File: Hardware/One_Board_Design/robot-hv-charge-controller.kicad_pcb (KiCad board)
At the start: 2 copper layers, 100 x 100 mm, 132 parts, among them J1 USB2.0_16P, J2 UART_CONN, J3 XT30PW-M, J4 Conn_01x02, J5 XT60PW-M, J6 Conn_01x02, J7 XT60PW-M, J8 Conn_01x03, J9 Conn_01x02, Q2 2SD882, Q3 BC817, Q4 BC817, Q5 2SD882, Q6 2SD882, Q7 MJD41CT4G, SW1 ENABLE, U1 TCAN3414DR, U10 LTV-356T, U11 LTV-356T, U12 LTV-356T, U13 LTV-356T, U14 LTV-356T, U15 CH340C, U2 INA240A1PW, U3 MAX3485, U4 ESP32-WROOM-32E, U5 USBLC6-2SC6, U6 LTV-356T, U7 TLV1117-33, U8 HF116F-80/24-1HTF, U9 LV14340DDAR

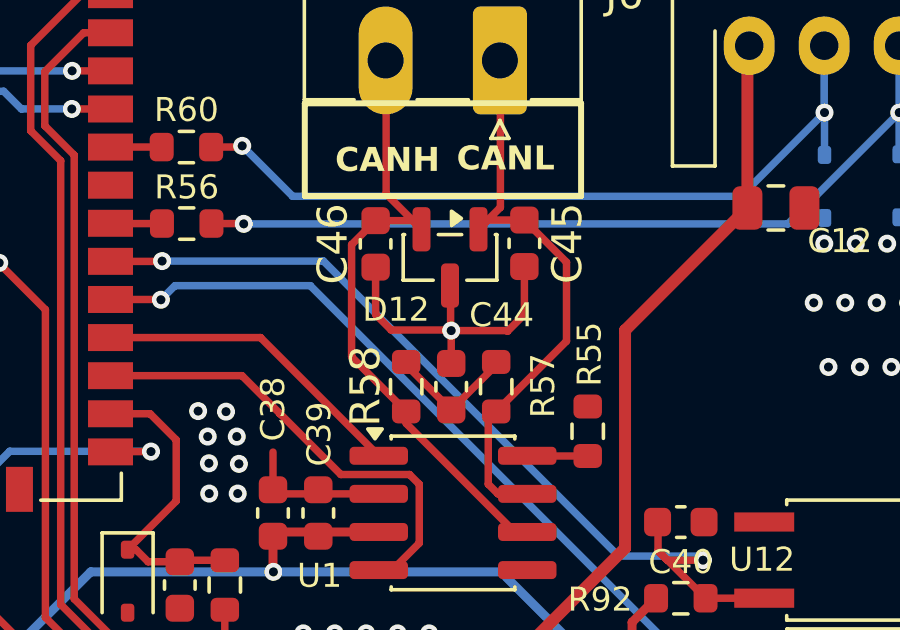
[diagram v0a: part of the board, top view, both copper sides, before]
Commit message: refactor(hardware): move KiCad project into One_Board_Design/
Relocate the single-board KiCad project (root schematic, five hierarchical sheets, PCB, project file, and library tables) into Hardware/One_Board_Design/ so the shared symbols, footprints, and 3D models stay in Hardware/libraries/.

Update library tables and 3D model references to use \/../libraries/... so the moved project resolves the shared library location correctly. Replace SparkFun symbol references with the equivalent KiCad standard symbols. Add One_Board_Design README documenting the shared-library layout.

Ultraworked with [Sisyphus](https://github.com/code-yeongyu/oh-my-openagent)

Co-authored-by: Sisyphus <clio-agent@sisyphuslabs.ai>
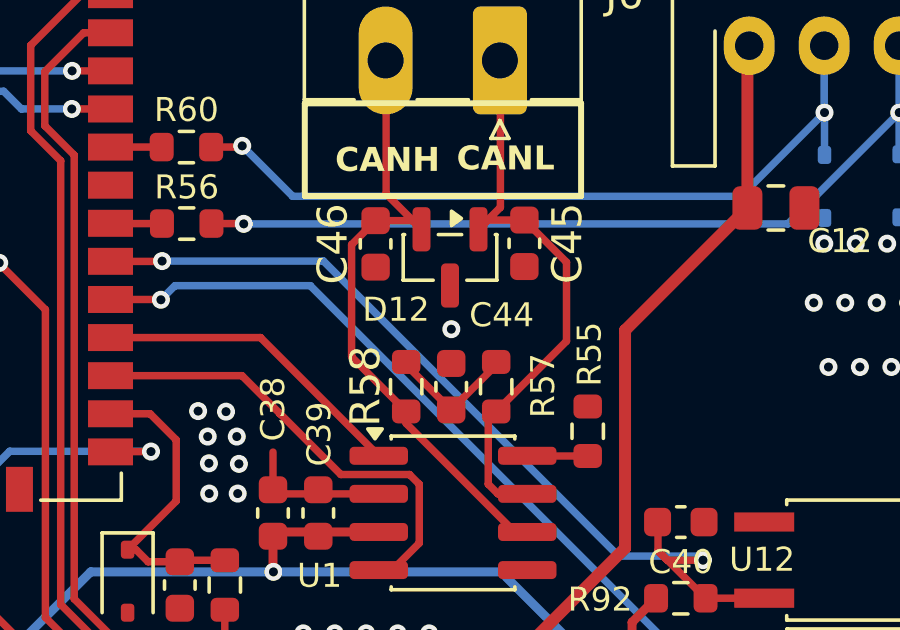
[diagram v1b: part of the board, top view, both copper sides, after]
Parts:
- R41, R49, R50: footprint CSS2H_2512R_1L00F:RES_1L00x_BRN -> RobotChargeController:RES_1L00x_BRN
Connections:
- C45 pad 2: Net-(C45-Pad2) -> GND
- C46 pad 1: Net-(C45-Pad2) -> GND
- J8 pad 1: DO1_SINK -> DO3_SINK
- J8 pad 3: DO3_SINK -> DO1_SINK
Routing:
- net GND: track 173.0 -> 161.8 mm
